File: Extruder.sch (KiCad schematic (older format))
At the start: 2 parts, among them J17 Probe, J18 Extruder Heater

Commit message: Finished the schematics wiring and reset the routing.
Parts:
- J17: footprint Connector_PinHeader_2.54mm:PinHeader_1x02_P2.54mm_Vertical -> kicad-molex-sl-footprints:Molex-SL-2POS
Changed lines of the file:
@@
 F 0 "J17" H 2450 4217 50  0000 C CNN
 F 1 "Probe" H 2450 4126 50  0000 C CNN
-F 2 "Connector_PinHeader_2.54mm:PinHeader_1x02_P2.54mm_Vertical" H 2400 4000 50  0001 C CNN
+F 2 "kicad-molex-sl-footprints:Molex-SL-2POS" H 2400 4000 50  0001 C CNN
 F 3 "~" H 2400 4000 50  0001 C CNN
 	1    2400 4000

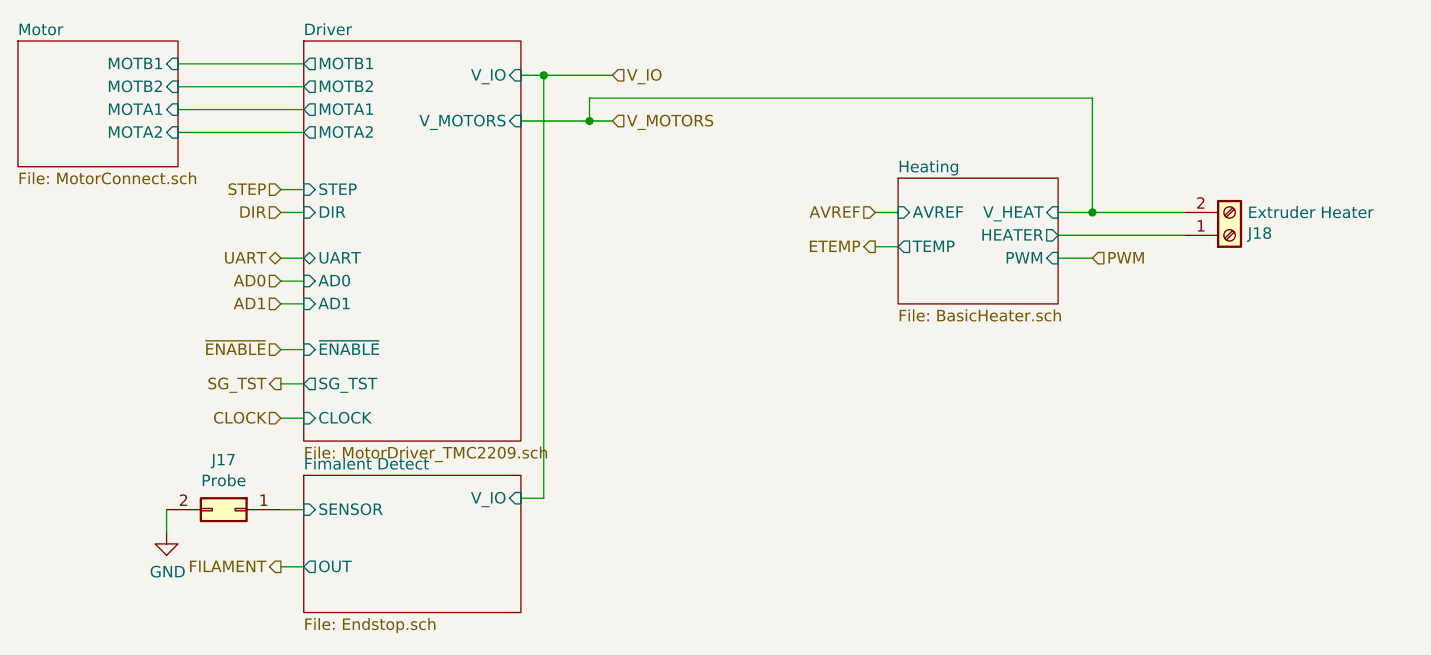
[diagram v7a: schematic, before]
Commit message: Added pul-ups on the UART ports and series resistors for protection.
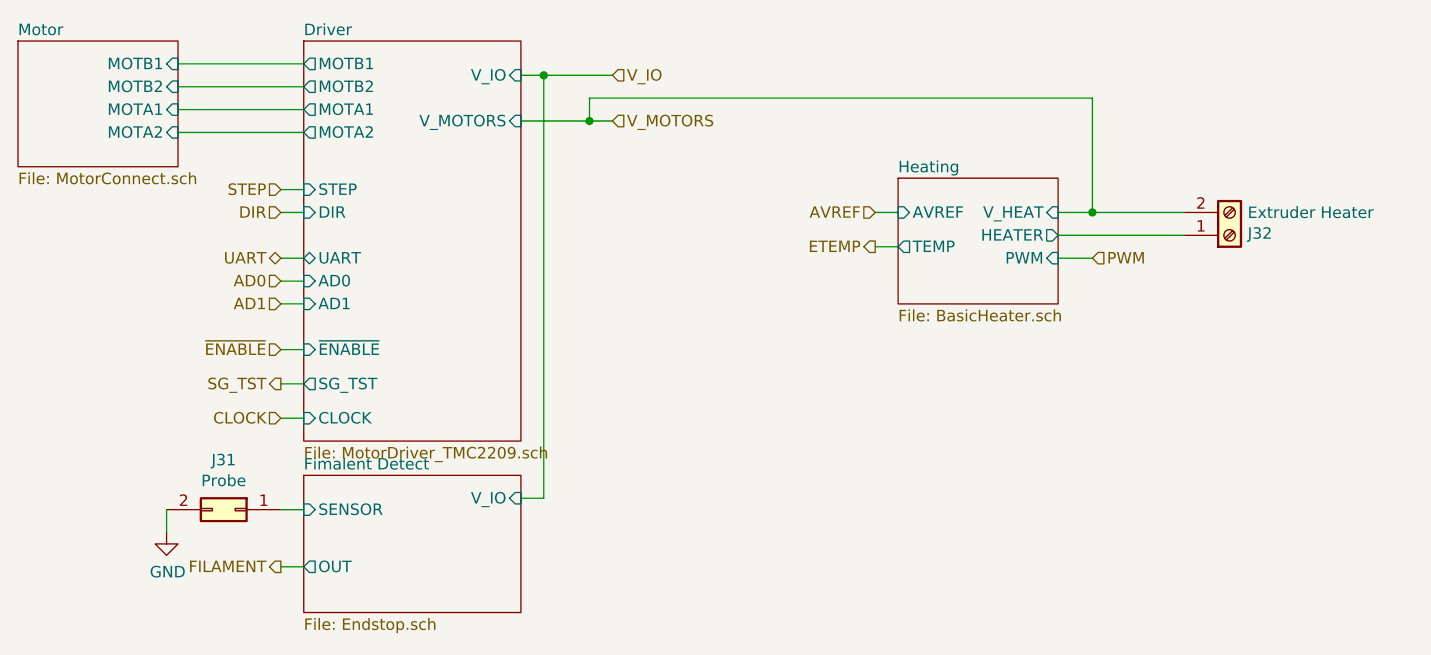
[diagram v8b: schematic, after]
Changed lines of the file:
@@
 AR Path="/5AC337B6/5ACBE919/5AD4BF35" Ref="J17"  Part="1"
 AR Path="/5AC337B6/5AD9F95A/5AD4BF35" Ref="J31"  Part="1"
-F 0 "J17" H 2450 4217 50  0000 C CNN
+F 0 "J31" H 2450 4217 50  0000 C CNN
 F 1 "Probe" H 2450 4126 50  0000 C CNN
 F 2 "kicad-molex-sl-footprints:Molex-SL-2POS" H 2400 4000 50  0001 C CNN
@@
 AR Path="/5AC337B6/5ACBE919/5AD4C143" Ref="#PWR022"  Part="1"
 AR Path="/5AC337B6/5AD9F95A/5AD4C143" Ref="#PWR067"  Part="1"
-F 0 "#PWR022" H 2100 3850 50  0001 C CNN
+F 0 "#PWR067" H 2100 3850 50  0001 C CNN
 F 1 "GND" H 2105 3927 50  0000 C CNN
 F 2 "" H 2100 4100 50  0001 C CNN
@@
 AR Path="/5AC337B6/5ACBE919/5AD53BDD" Ref="J18"  Part="1"
 AR Path="/5AC337B6/5AD9F95A/5AD53BDD" Ref="J32"  Part="1"
-F 0 "J18" H 6829 2792 50  0000 L CNN
+F 0 "J32" H 6829 2792 50  0000 L CNN
 F 1 "Extruder Heater" H 6829 2701 50  0000 L CNN
 F 2 "PrntrBoardV1:TerminalBlock_Phoenix_PT-1,5-2-3.5-H_1x02_P3.50mm_Horizontal" H 6750 2800 50  0001 C CNN
